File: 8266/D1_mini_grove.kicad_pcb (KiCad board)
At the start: 2 copper layers, 25.7 x 34.3 mm, 9 parts, among them P1 Connector_Generic:Conn_01x08, P2 Connector_Generic:Conn_01x08

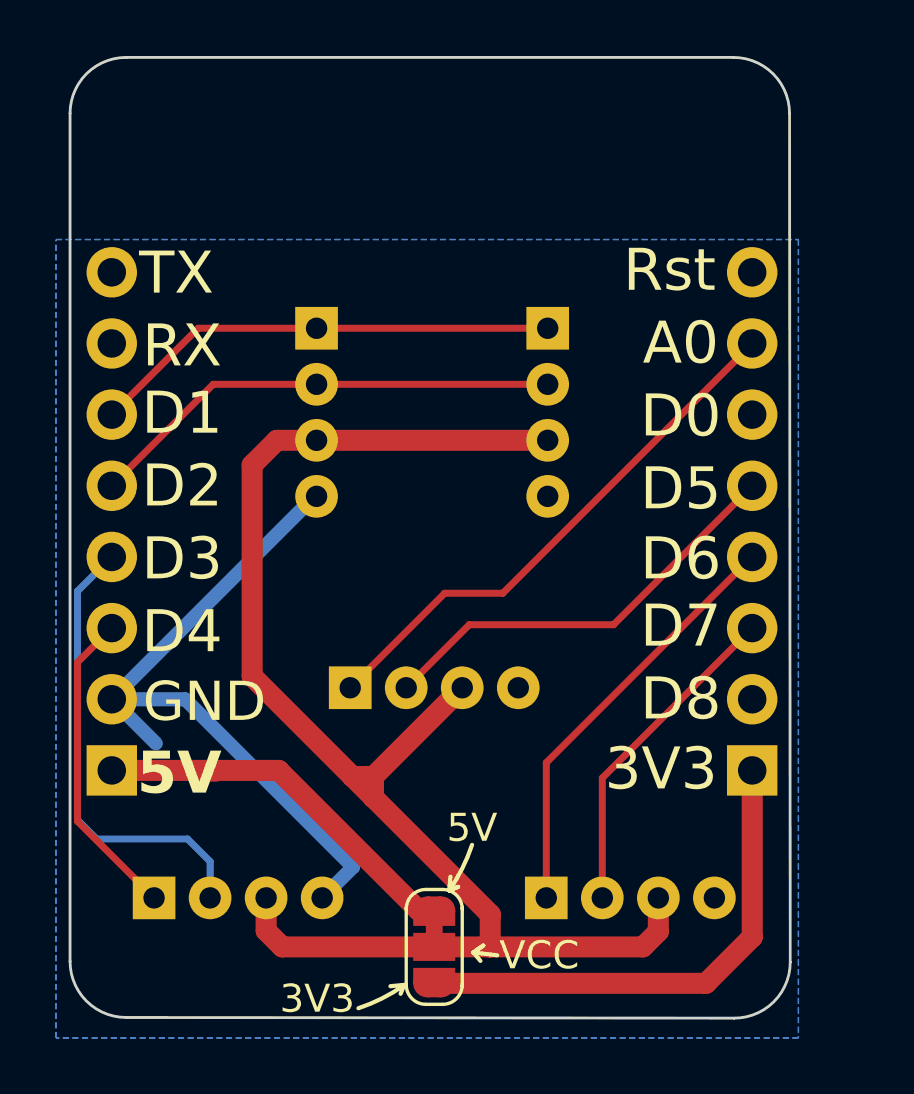
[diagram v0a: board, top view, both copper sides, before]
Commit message: Added a switch for VCC selector instead of solder bridge.. its tight but itll work
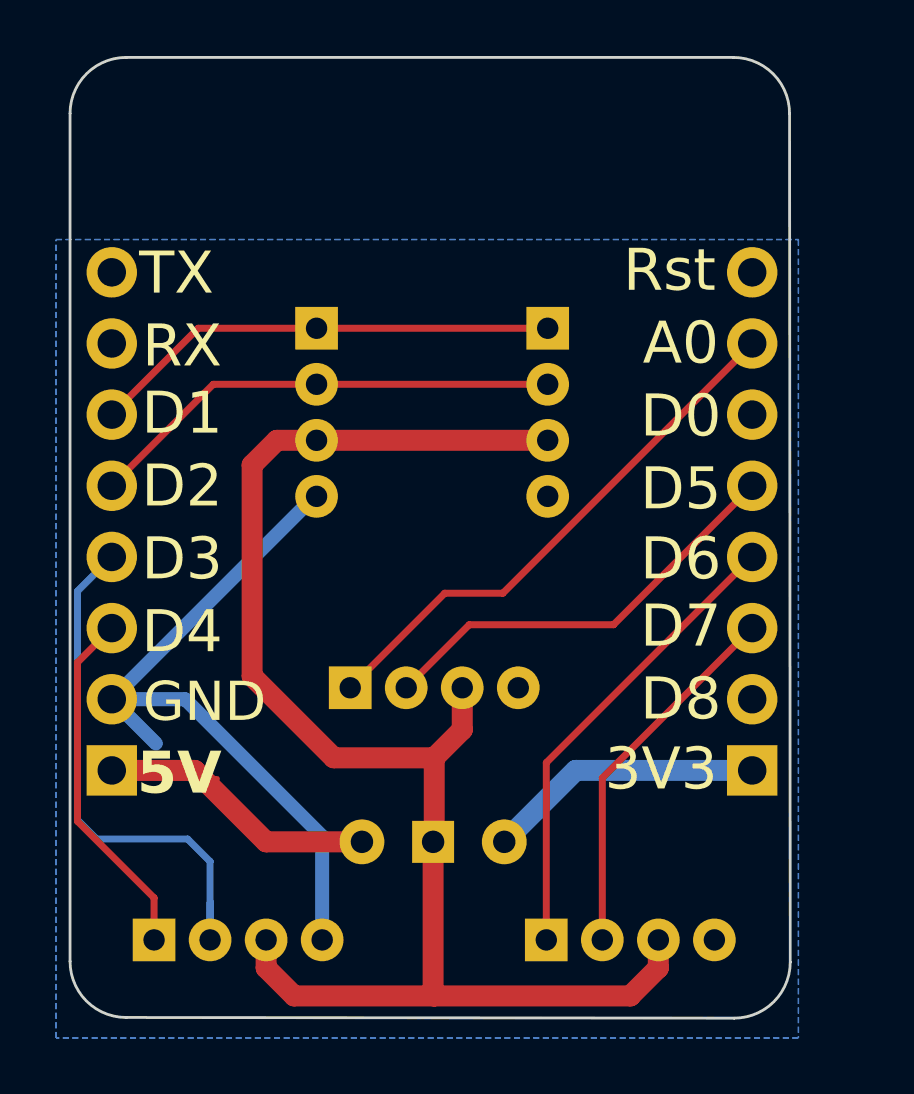
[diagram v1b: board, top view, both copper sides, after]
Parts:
- removed VCC: SolderJumper_3_Bridged12, Jumper:SolderJumper-3_P1.3mm_Bridged12_RoundedPad1.0x1.5mm_NumberLabels
- added SW1: SW_Wuerth_450301014042, Button_Switch_THT:SW_Slide-03_Wuerth-WS-SLTV_10x2.5x6.4_P2.54mm, F.Cu at (139.0, 106.5)
- moved 3_4 1.50 mm to (129.0, 110.0)
- moved 5_6 1.50 mm to (143.0, 110.0)
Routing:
- net +3V3: track 18.0 -> 9.91 mm
- net +5V: track 13.6 -> 9.99 mm
- net /D3: track 16.7 -> 19.4 mm
- net TX1_D4: track 11.3 -> 12.8 mm
- net /D7: track 11.8 -> 13.3 mm
- net /D6: track 15.2 -> 16.7 mm
- net GND: track 25.2 -> 25.8 mm
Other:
- board text added: "VCC:"

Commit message: Messing with silkscreen, mostly
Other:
- board text added: "VCC"
- board text removed: "VCC:"
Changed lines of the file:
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@@
 	)
 	(gr_line
-		(start 132.45 105.4)
-		(end 129.75 106.1)
-		(stroke
-			(width 0.15)
-			(type default)
-		)
-		(layer "B.SilkS")
+		(start 131.47 111.43)
+		(end 131.28 111.35)
+		(stroke
+			(width 0.15)
+			(type solid)
+		)
+		(layer "F.SilkS")
+	)
+	(gr_line
+		(start 131.28 111.35)
+		(end 131.27 111.538636)
+		(stroke
+			(width 0.15)
+			(type solid)
+		)
+		(layer "F.SilkS")
+	)
+	(gr_line
+		(start 130.5 111.400002)
+		(end 130.155379 111.445626)
+		(stroke
+			(width 0.15)
+			(type solid)
+		)
+		(layer "F.SilkS")
+	)
+	(gr_line
+		(start 130.155379 111.445626)
+		(end 130.155379 111.700002)
+		(stroke
+			(width 0.15)
+			(type solid)
+		)
+		(layer "F.SilkS")
+	)
+	(gr_arc
+		(start 132.300002 112.2)
+		(mid 131.190075 111.92975)
+		(end 130.155379 111.445624)
+		(stroke
+			(width 0.15)
+			(type solid)
+		)
+		(layer "F.SilkS")
+	)
+	(gr_line
+		(start 131.27 111.538636)
+		(end 131.47 111.43)
+		(stroke
+			(width 0.15)
+			(type solid)
+		)
+		(layer "F.SilkS")
+	)
+	(gr_arc
+		(start 132.3 112.2)
+		(mid 131.794252 111.92894)
+		(end 131.373637 111.538636)
+		(stroke
+			(width 0.15)
+			(type solid)
+		)
+		(layer "F.SilkS")
+	)
+	(gr_line
+		(start 130.155379 111.700002)
+		(end 130.5 111.400002)
+		(stroke
+			(width 0.15)
+			(type solid)
+		)
+		(layer "F.SilkS")
 	)
 	(gr_line
@@
 		(layer "B.SilkS")
 	)
+	(gr_line
+		(start 130.590881 105.299223)
+		(end 130.63 105.85)
+		(stroke
+			(width 0.5)
+			(type solid)
+		)
+		(layer "B.SilkS")
+	)
 	(gr_arc
 		(start 141.508092 84.339906)
@@
 		(end 143.134986 85.158629)
 		(stroke
-			(width 0.15)
-			(type default)
+			(width 0.3)
+			(type solid)
 		)
 		(layer "B.SilkS")
@@
 	)
 	(gr_line
-		(start 131.6 106.05)
-		(end 131.65 105.8)
-		(stroke
-			(width 0.15)
-			(type default)
-		)
-		(layer "B.SilkS")
-	)
-	(gr_line
-		(start 132.45 105.4)
-		(end 131.6 106.05)
-		(stroke
-			(width 0.15)
-			(type default)
-		)
-		(layer "B.SilkS")
-	)
-	(gr_line
-		(start 131.65 105.8)
-		(end 131.85 106.05)
+		(start 130.590881 105.299223)
+		(end 131.1 105.299223)
+		(stroke
+			(width 0.5)
+			(type solid)
+		)
+		(layer "B.SilkS")
+	)
+	(gr_arc
+		(start 133.98 106.7)
+		(mid 132.1595 106.304318)
+		(end 130.590881 105.299223)
+		(stroke
+			(width 0.5)
+			(type solid)
+		)
+		(layer "B.SilkS")
+	)
+	(gr_line
+		(start 138.94 108.74)
+		(end 138.62 109.06)
+		(stroke
+			(width 0.15)
+			(type default)
+		)
+		(layer "B.SilkS")
+	)
+	(gr_line
+		(start 138.94 109.74)
+		(end 138.94 108.74)
 		(stroke
 			(width 0.15)
@@
 	(gr_line
 		(start 143.134986 85.158629)
-		(end 142.851165 84.690398)
-		(stroke
-			(width 0.15)
-			(type default)
-		)
-		(layer "B.SilkS")
-	)
-	(gr_line
-		(start 130 106.25)
-		(end 129.75 106.1)
-		(stroke
-			(width 0.15)
-			(type default)
-		)
-		(layer "B.SilkS")
-	)
-	(gr_line
-		(start 129.9 105.85)
-		(end 130 106.25)
-		(stroke
-			(width 0.15)
-			(type default)
-		)
-		(layer "B.SilkS")
-	)
-	(gr_line
-		(start 129.9 105.85)
-		(end 129.75 106.1)
+		(end 142.97 84.7)
+		(stroke
+			(width 0.3)
+			(type solid)
+		)
+		(layer "B.SilkS")
+	)
+	(gr_line
+		(start 146.79 105.090506)
+		(end 146.12 105.1)
+		(stroke
+			(width 0.5)
+			(type solid)
+		)
+		(layer "B.SilkS")
+	)
+	(gr_line
+		(start 138.94 108.74)
+		(end 139.25 109.07)
 		(stroke
 			(width 0.15)
@@
 	(gr_line
 		(start 143.134986 85.158629)
-		(end 142.851165 85.190398)
-		(stroke
-			(width 0.15)
-			(type default)
-		)
-		(layer "B.SilkS")
-	)
-	(gr_line
-		(start 131.85 106.05)
-		(end 131.6 106.05)
-		(stroke
-			(width 0.15)
-			(type default)
+		(end 142.63 85.190398)
+		(stroke
+			(width 0.3)
+			(type solid)
 		)
 		(layer "B.SilkS")
@@
 		(layer "B.SilkS")
 	)
-	(gr_line
-		(start 129.75 106.1)
-		(end 129.9 105.85)
-		(stroke
-			(width 0.15)
-			(type default)
+	(gr_arc
+		(start 146.792873 105.093577)
+		(mid 145.405557 106.122492)
+		(end 143.821056 106.81)
+		(stroke
+			(width 0.5)
+			(type solid)
+		)
+		(layer "B.SilkS")
+	)
+	(gr_line
+		(start 146.79 105.090506)
+		(end 146.85 105.66)
+		(stroke
+			(width 0.5)
+			(type solid)
 		)
 		(layer "B.SilkS")
@@
 		(start 127.325 108.025)
 		(end 127.375 108.175)
-		(stroke
-			(width 0.15)
-			(type default)
-		)
-		(layer "B.SilkS")
-	)
-	(gr_line
-		(start 139.95 104.7)
-		(end 132.45 105.4)
 		(stroke
 			(width 0.15)
@@
 		)
 	)
+	(gr_text " KEEP HIGH AT BOOT!"
+		(at 132.08 112.48 0)
+		(layer "F.SilkS")
+		(effects
+			(font
+				(size 0.8 0.6)
+				(thickness 0.125)
+			)
+			(justify left bottom)
+		)
+	)
 	(gr_text "D1"
 		(at 130 91.2 0)
@@
 		)
 	)
-	(gr_text "VCC:"
-		(at 138.5 111.3 270)
-		(layer "B.SilkS")
-		(effects
-			(font
-				(size 0.8 0.8)
-				(thickness 0.15)
-			)
-			(justify left bottom mirror)
-		)
-	)
-	(gr_text "5V"
-		(at 138.3 109.7 0)
-		(layer "B.SilkS")
-		(effects
-			(font
-				(size 0.8 0.8)
-				(thickness 0.15)
+	(gr_text "VCC"
+		(at 138.32 112.54 270)
+		(layer "B.SilkS")
+		(effects
+			(font
+				(size 0.9 0.9)
+				(thickness 0.2)
+				(bold yes)
 			)
 			(justify left bottom mirror)
@@
 		)
 	)
-	(gr_text " KEEP HIGH AT BOOT!"
-		(at 141.425 104.5 5)
-		(layer "B.SilkS")
-		(effects
-			(font
-				(size 0.8 0.6)
-				(thickness 0.125)
-			)
-			(justify left bottom mirror)
-		)
-	)
 	(gr_text "I2C"
 		(at 141.5 85.175 -0)
@@
 			(font
 				(size 1 1)
-				(thickness 0.15)
-			)
-			(justify left bottom mirror)
-		)
-	)
-	(gr_text "3V3"
-		(at 141.9 109.7 0)
-		(layer "B.SilkS")
-		(effects
-			(font
-				(size 0.8 0.8)
 				(thickness 0.15)
 			)
@@
 		)
 	)
+	(group ""
+		(members "6665ba5d-28bd-45f5-a118-b25ec488c116" "ccf26901-8587-4094-8bd9-66620f58f2cf"
+			"de09b03a-0e44-4ec1-953f-4cd3571b92aa"
+		)
+	)

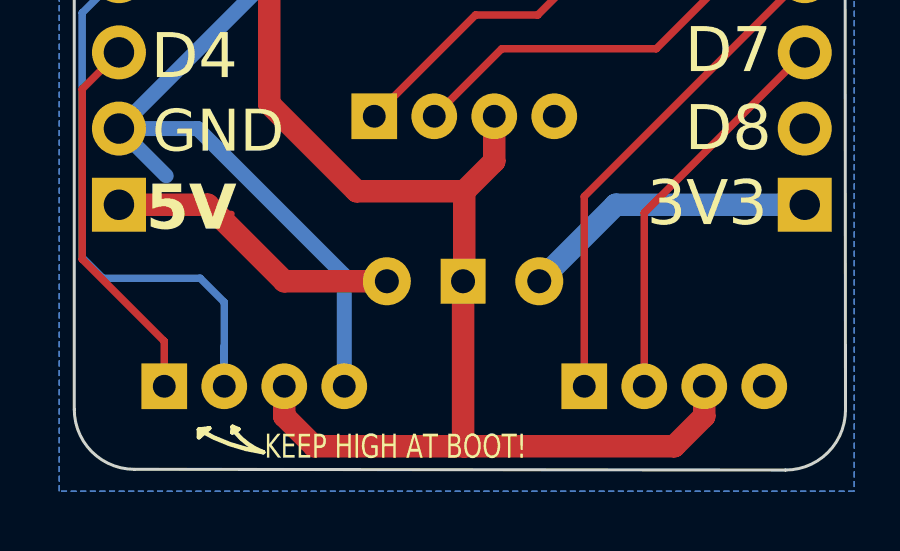
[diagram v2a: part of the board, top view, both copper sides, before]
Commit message: Production run for 8266 board as well.
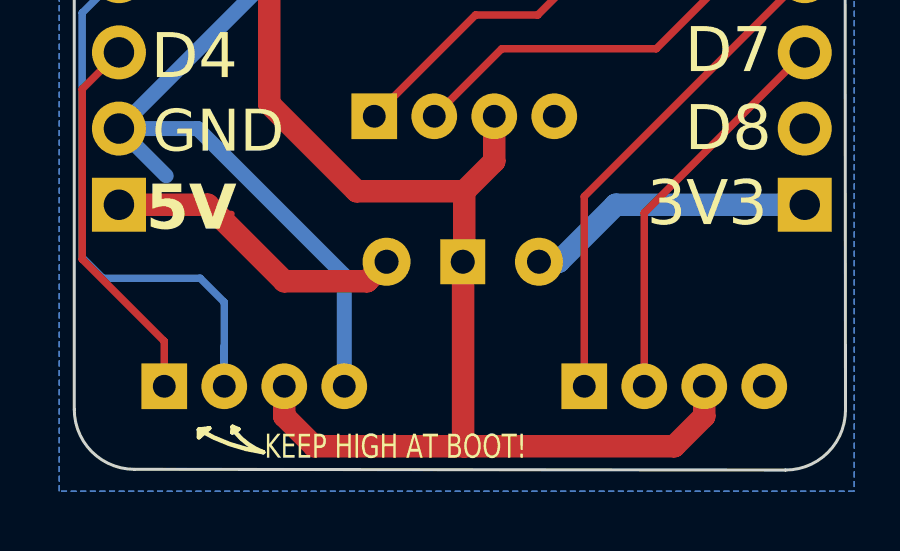
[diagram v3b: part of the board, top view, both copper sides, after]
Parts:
- SW1: moved to B.Cu
- moved SW1 0.65 mm to (138.9, 105.8)

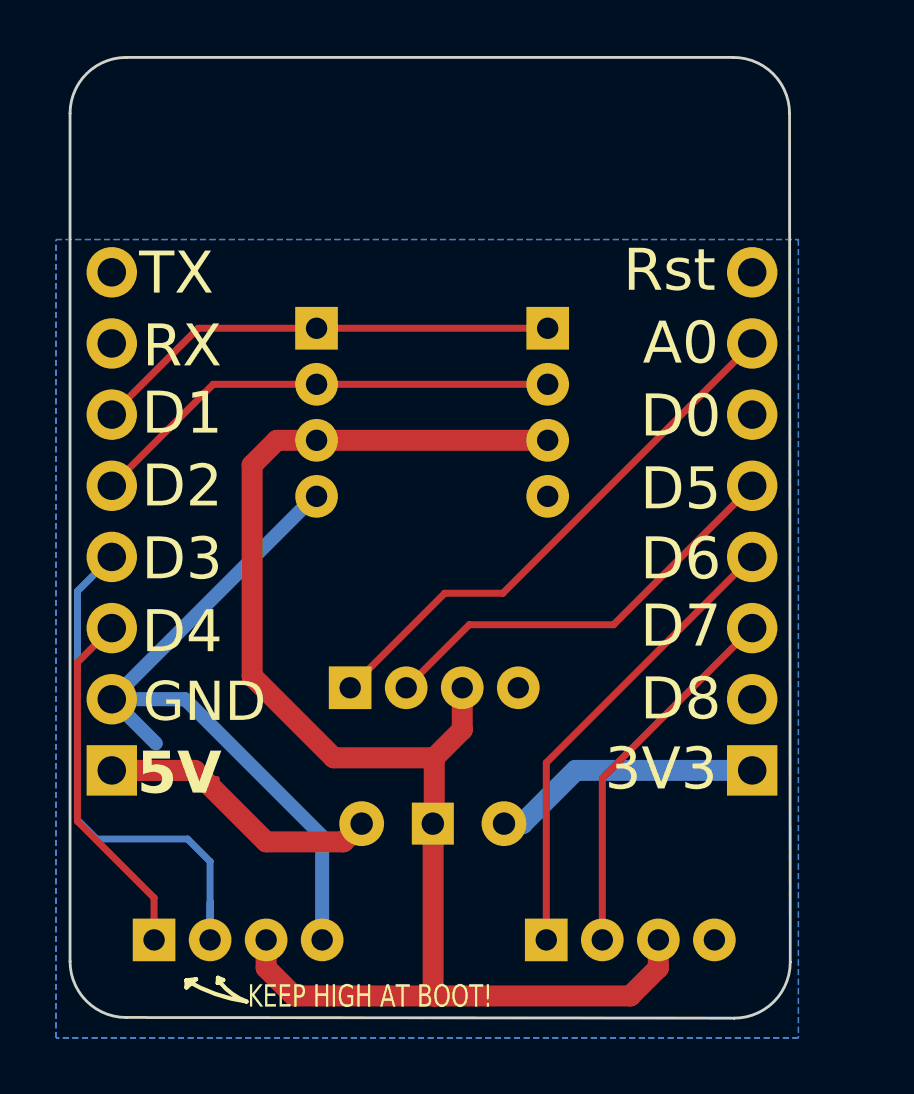
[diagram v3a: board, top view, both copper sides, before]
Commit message: Set 3D model dir to relaive path, flipped entire 8266 board around so it sits right in my mind
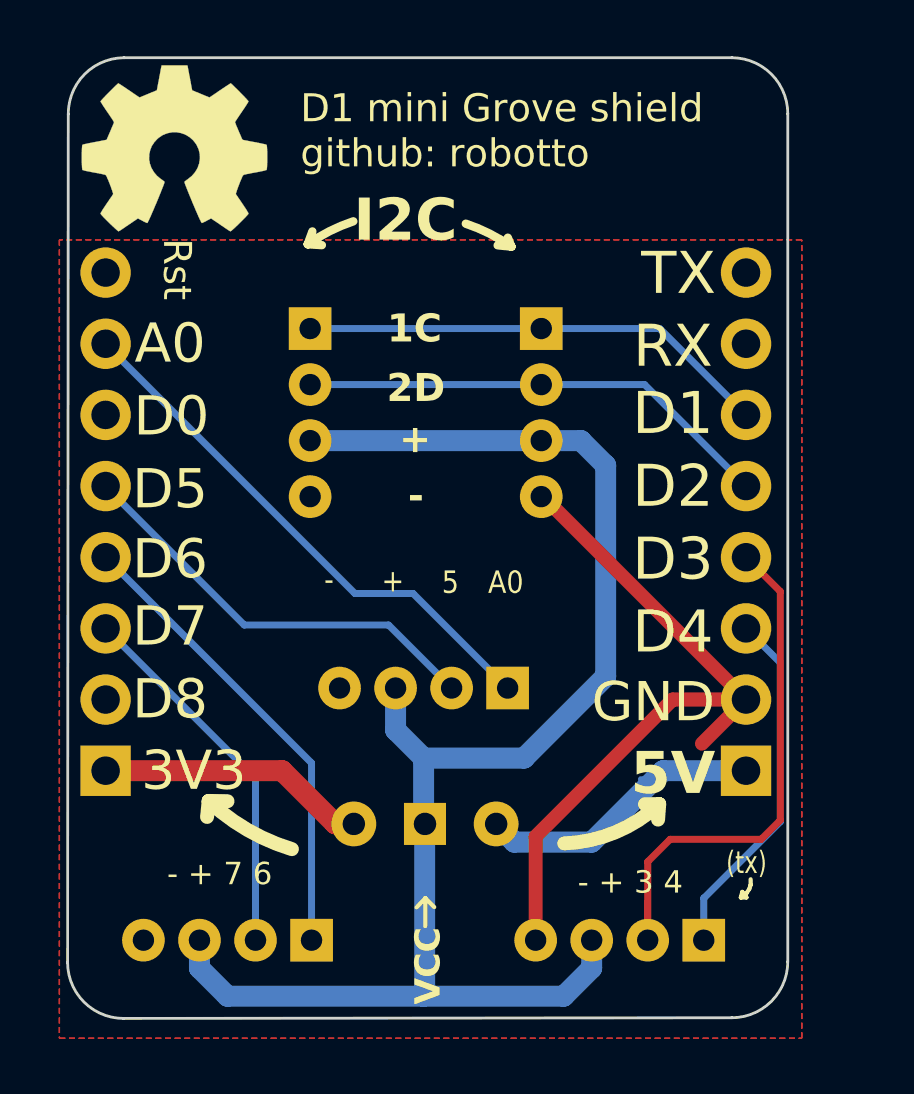
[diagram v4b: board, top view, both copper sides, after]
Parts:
- 1_2_IIC1, 1_2_IIC2, 3_4, 5_6, A0_7, REF**, SW1: moved to F.Cu
- P1, P2: moved to B.Cu
- moved P2 23.1 mm to (127.3, 104.0), turned to 0 degrees
- moved P1 22.6 mm to (150.1, 104.0), turned to 0 degrees
- moved 3_4 19.6 mm to (148.6, 110.0)
- moved REF** 18.2 mm to (129.7, 81.8), turned to 0 degrees
- moved 1_2_IIC2 8.48 mm to (134.6, 88.2), turned to 0 degrees
- moved 5_6 8.38 mm to (134.6, 110.0)
- moved 1_2_IIC1 8.02 mm to (142.8, 88.2), turned to 0 degrees
- moved A0_7 5.62 mm to (141.6, 101.0)
- moved SW1 0.28 mm to (138.7, 105.9), turned to 0 degrees
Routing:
- added copper zone on F.Cu, net GND
- removed copper zone on B.Cu, net GND
